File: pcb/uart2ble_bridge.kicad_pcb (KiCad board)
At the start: 2 copper layers, 10.6 x 21.8 mm, 14 parts, among them P1 CONN_01X04, P2 SWDCLK, P3 SDWIO, U1 BVMCN5103-BK

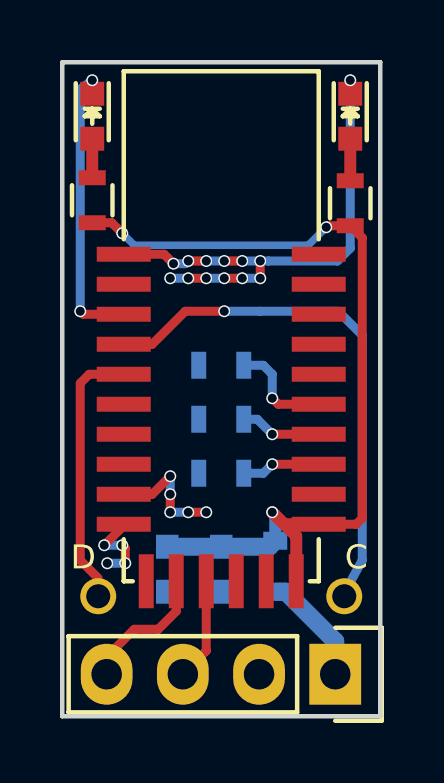
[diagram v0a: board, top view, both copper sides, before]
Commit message: LEDを二つともマイコンから操作できるように変更
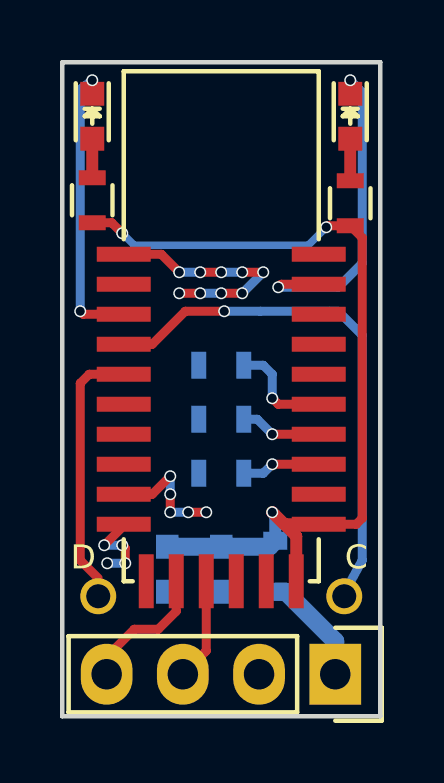
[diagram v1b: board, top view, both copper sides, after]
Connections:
- D3 pad 1: GND -> Net-(D3-Pad1)
- U1 pad 25: (no net) -> Net-(D3-Pad1)
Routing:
- net Net-(D3-Pad1): track 0.00 -> 11.4 mm, vias 0 -> 2
- net GND: track 24.9 -> 15.2 mm, vias 22 -> 18
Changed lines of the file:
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@@
     (links 29)
     (no_connects 0)
-    (area 138.125 89.414285 161.35 123.400001)
+    (area 139.924999 94.524999 150.675001 116.475001)
     (thickness 1.6)
     (drawings 8)
-    (tracks 126)
+    (tracks 121)
     (zones 0)
     (modules 14)
-    (nets 14)
+    (nets 15)
   )
   (page A4)
@@
   )
   (setup
-    (last_trace_width 0.25)
+    (last_trace_width 0.3)
     (user_trace_width 0.2)
     (user_trace_width 0.3)
@@
   (net 12 "Net-(JP2-Pad2)")
   (net 13 "Net-(JP3-Pad2)")
+  (net 14 "Net-(D3-Pad1)")
   (net_class Default "これは標準のネット クラスです。"
     (clearance 0.2)
@@
     (add_net "Net-(D2-Pad1)")
     (add_net "Net-(D2-Pad2)")
+    (add_net "Net-(D3-Pad1)")
     (add_net "Net-(D3-Pad2)")
     (add_net "Net-(JP1-Pad2)")
@@
       (net 6 "Net-(D3-Pad2)"))
     (pad 1 smd rect (at -0.7493 0 90) (size 0.79756 0.79756) (layers F.Cu F.Paste F.Mask)
-      (net 2 GND))
+      (net 14 "Net-(D3-Pad1)"))
     (model LEDs.3dshapes/LED_0603.wrl
       (at (xyz 0 0 0))
@@
     (pad 23 smd rect (at 3.25 -6) (size 1.8 0.5) (layers F.Cu F.Paste F.Mask))
     (pad 24 smd rect (at 3.25 -7) (size 1.8 0.5) (layers F.Cu F.Paste F.Mask))
-    (pad 25 smd rect (at 3.25 -8) (size 1.8 0.5) (layers F.Cu F.Paste F.Mask))
+    (pad 25 smd rect (at 3.25 -8) (size 1.8 0.5) (layers F.Cu F.Paste F.Mask)
+      (net 14 "Net-(D3-Pad1)"))
     (pad 26 smd rect (at 3.25 -9) (size 1.8 0.5) (layers F.Cu F.Paste F.Mask)
       (net 2 GND))
@@
   (segment (start 146.9 110.75) (end 147.1 110.55) (width 0.6) (layer B.Cu) (net 1))
   (segment (start 143.5 110.75) (end 145.3 110.75) (width 0.6) (layer B.Cu) (net 1))
-  (segment (start 146.882842 101.22501) (end 146.6 101.22501) (width 0.3) (layer B.Cu) (net 2))
-  (segment (start 149.6 100.8) (end 149.17499 101.22501) (width 0.3) (layer B.Cu) (net 2))
-  (segment (start 146 101.22501) (end 146.6 101.22501) (width 0.3) (layer B.Cu) (net 2))
-  (segment (start 143.707398 101.313908) (end 144.111102 101.313908) (width 0.3) (layer B.Cu) (net 2))
-  (segment (start 144.111102 101.313908) (end 144.2 101.22501) (width 0.3) (layer B.Cu) (net 2))
-  (via (at 146.6 101.22501) (size 0.4) (drill 0.3) (layers F.Cu B.Cu) (net 2))
-  (via (at 146 101.22501) (size 0.4) (drill 0.3) (layers F.Cu B.Cu) (net 2))
-  (segment (start 149.17499 101.22501) (end 146.882842 101.22501) (width 0.3) (layer B.Cu) (net 2))
-  (via (at 145.4 101.22501) (size 0.4) (drill 0.3) (layers F.Cu B.Cu) (net 2))
-  (via (at 144.8 101.22501) (size 0.4) (drill 0.3) (layers F.Cu B.Cu) (net 2))
-  (segment (start 149.6 95.2) (end 149.6 100.8) (width 0.3) (layer B.Cu) (net 2))
-  (segment (start 144.8 101.22501) (end 145.4 101.22501) (width 0.3) (layer B.Cu) (net 2))
-  (via (at 144.2 101.22501) (size 0.4) (drill 0.3) (layers F.Cu B.Cu) (net 2))
-  (segment (start 144.2 101.22501) (end 144.8 101.22501) (width 0.3) (layer F.Cu) (net 2))
-  (segment (start 146.6 101.8) (end 146.6 101.22501) (width 0.3) (layer F.Cu) (net 2))
-  (segment (start 145.4 101.22501) (end 146 101.22501) (width 0.3) (layer F.Cu) (net 2))
-  (segment (start 143.39349 101) (end 143.507399 101.113909) (width 0.3) (layer F.Cu) (net 2))
-  (segment (start 143.507399 101.113909) (end 143.707398 101.313908) (width 0.3) (layer F.Cu) (net 2))
-  (segment (start 142.05 101) (end 143.39349 101) (width 0.3) (layer F.Cu) (net 2))
-  (via (at 143.707398 101.313908) (size 0.4) (drill 0.3) (layers F.Cu B.Cu) (net 2))
-  (segment (start 149.6 95.6507) (end 149.6 95.2) (width 0.3) (layer F.Cu) (net 2))
-  (via (at 149.6 95.2) (size 0.4) (drill 0.3) (layers F.Cu B.Cu) (net 2))
+  (segment (start 142.05 101) (end 143.3 101) (width 0.3) (layer F.Cu) (net 2))
+  (via (at 143.9 102.3) (size 0.4) (drill 0.3) (layers F.Cu B.Cu) (net 2))
+  (segment (start 144.6 102.3) (end 143.9 102.3) (width 0.3) (layer F.Cu) (net 2))
+  (via (at 144.6 102.3) (size 0.4) (drill 0.3) (layers F.Cu B.Cu) (net 2))
+  (segment (start 145.3 102.3) (end 144.6 102.3) (width 0.3) (layer B.Cu) (net 2))
+  (via (at 145.3 102.3) (size 0.4) (drill 0.3) (layers F.Cu B.Cu) (net 2))
+  (segment (start 146 102.3) (end 145.3 102.3) (width 0.3) (layer F.Cu) (net 2))
+  (via (at 146 102.3) (size 0.4) (drill 0.3) (layers F.Cu B.Cu) (net 2))
+  (segment (start 146.7 101.6) (end 146 102.3) (width 0.3) (layer B.Cu) (net 2))
+  (via (at 146.7 101.6) (size 0.4) (drill 0.3) (layers F.Cu B.Cu) (net 2))
+  (segment (start 146 101.6) (end 146.7 101.6) (width 0.3) (layer F.Cu) (net 2))
+  (via (at 146 101.6) (size 0.4) (drill 0.3) (layers F.Cu B.Cu) (net 2))
+  (segment (start 145.3 101.6) (end 146 101.6) (width 0.3) (layer B.Cu) (net 2))
+  (via (at 145.3 101.6) (size 0.4) (drill 0.3) (layers F.Cu B.Cu) (net 2))
+  (segment (start 144.6 101.6) (end 145.3 101.6) (width 0.3) (layer F.Cu) (net 2))
+  (via (at 144.6 101.6) (size 0.4) (drill 0.3) (layers F.Cu B.Cu) (net 2))
+  (segment (start 143.9 101.6) (end 144.6 101.6) (width 0.3) (layer B.Cu) (net 2))
+  (via (at 143.9 101.6) (size 0.4) (drill 0.3) (layers F.Cu B.Cu) (net 2))
+  (segment (start 143.3 101) (end 143.9 101.6) (width 0.3) (layer F.Cu) (net 2))
   (segment (start 141.5 111.3) (end 142.1 111.3) (width 0.3) (layer B.Cu) (net 2))
   (via (at 142.1 111.3) (size 0.4) (drill 0.3) (layers F.Cu B.Cu) (net 2))
@@
   (segment (start 141.4 110.7) (end 142.05 110.05) (width 0.3) (layer F.Cu) (net 2) (status 10))
   (via (at 141.5 111.3) (size 0.4) (drill 0.3) (layers F.Cu B.Cu) (net 2))
-  (segment (start 149.6 95.6507) (end 149.6 95.5) (width 0.3) (layer F.Cu) (net 2))
-  (via (at 143.6 101.8) (size 0.4) (drill 0.3) (layers F.Cu B.Cu) (net 2))
-  (via (at 146.6 101.8) (size 0.4) (drill 0.3) (layers F.Cu B.Cu) (net 2))
-  (segment (start 146.6 101.8) (end 146 101.8) (width 0.3) (layer B.Cu) (net 2))
-  (via (at 146 101.8) (size 0.4) (drill 0.3) (layers F.Cu B.Cu) (net 2))
-  (segment (start 146 101.8) (end 145.4 101.8) (width 0.3) (layer F.Cu) (net 2))
-  (via (at 145.4 101.8) (size 0.4) (drill 0.3) (layers F.Cu B.Cu) (net 2))
-  (segment (start 145.4 101.8) (end 144.8 101.8) (width 0.3) (layer B.Cu) (net 2))
-  (via (at 144.8 101.8) (size 0.4) (drill 0.3) (layers F.Cu B.Cu) (net 2))
-  (segment (start 144.8 101.8) (end 144.2 101.8) (width 0.3) (layer F.Cu) (net 2))
-  (via (at 144.2 101.8) (size 0.4) (drill 0.3) (layers F.Cu B.Cu) (net 2))
-  (segment (start 144.2 101.8) (end 143.6 101.8) (width 0.3) (layer B.Cu) (net 2))
   (segment (start 142.8 111.9) (end 142.8 112.1) (width 0.3) (layer F.Cu) (net 2) (status 30))
   (segment (start 142.05 110) (end 142.05 110.05) (width 0.3) (layer F.Cu) (net 2) (status 30))
@@
   (via (at 147 105.8) (size 0.4) (drill 0.3) (layers F.Cu B.Cu) (net 13))
   (segment (start 147.2 106) (end 147 105.8) (width 0.3) (layer F.Cu) (net 13))
+  (segment (start 149.6 95.6507) (end 149.6 95.2) (width 0.3) (layer F.Cu) (net 14))
+  (segment (start 147.3 102) (end 148.55 102) (width 0.3) (layer F.Cu) (net 14))
+  (segment (start 147.2 102.1) (end 147.3 102) (width 0.3) (layer F.Cu) (net 14))
+  (via (at 147.2 102.1) (size 0.4) (drill 0.3) (layers F.Cu B.Cu) (net 14))
+  (segment (start 149.2 102.1) (end 147.2 102.1) (width 0.3) (layer B.Cu) (net 14))
+  (segment (start 150 101.3) (end 149.2 102.1) (width 0.3) (layer B.Cu) (net 14))
+  (segment (start 150 95.6) (end 150 101.3) (width 0.3) (layer B.Cu) (net 14))
+  (segment (start 149.6 95.2) (end 150 95.6) (width 0.3) (layer B.Cu) (net 14))
+  (via (at 149.6 95.2) (size 0.4) (drill 0.3) (layers F.Cu B.Cu) (net 14))
+  (segment (start 149.6 95.6507) (end 149.6 95.5) (width 0.3) (layer F.Cu) (net 14))
   (zone (net 2) (net_name GND) (layer B.Cu) (hatch edge 0.508)
     (connect_pads (clearance 0.2))
